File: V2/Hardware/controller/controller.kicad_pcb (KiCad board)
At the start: 2 copper layers, 45 parts, among them J0 Molex_PSU_F, J2 Flat_7seg_F, J3 Rpi_DATA_F_3.3V, Q0 BD139-16, Q1 BD139-16, Q2 BD139-16, Q3 BD139-16, Q4 BD139-16, Q5 BD139-16, Q6 BD139-16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

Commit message: Finish PCBs
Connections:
- net /DATA0 renamed /BIT_D
- J3 pad 2: /DATA1 -> Net-(J3-Pad2)
- J3 pad 3: /DATA2 -> /BIT_C
- J3 pad 4: /DATA3 -> /BIT_C
- J3 pad 5: Net-(J3-Pad5) -> /BIT_B
- J3 pad 6: Net-(J3-Pad6) -> /BIT_A
- R10 pad 2: /DATA1 -> /BIT_C
- R11 pad 2: /DATA2 -> /BIT_B
- R12 pad 2: /DATA3 -> /BIT_A
- U1 pad 7: /DATA1 -> /BIT_C
- U1 pad 8: /DATA2 -> /BIT_B
- U1 pad 9: /DATA3 -> /BIT_A
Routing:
- net /DATA2: track 87.7 -> 0.00 mm, vias 2 -> 0
- net /BIT_B: track 0.00 -> 80.8 mm, vias 0 -> 2
- net /BIT_A: track 0.00 -> 57.9 mm
- net /DATA3: track 52.5 -> 0.00 mm
- net /BIT_C: track 0.00 -> 51.4 mm
- net /DATA1: track 42.4 -> 0.00 mm

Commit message: Reinforce output
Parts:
- J2: footprint Connector_PinHeader_2.54mm:PinHeader_2x04_P2.54mm_Horizontal -> Connector_PinHeader_2.54mm:PinHeader_2x05_P2.54mm_Horizontal
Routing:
- net /+12V: track 183.1 -> 187.3 mm

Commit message: Export -pcbs
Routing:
- net Earth: track 212.7 -> 244.7 mm
- net /+12V: track 187.3 -> 216.8 mm
- net Net-(R0-Pad1): track 169.0 -> 184.9 mm
- net Net-(D5-Pad2): track 14.4 -> 26.7 mm
- net Net-(R18-Pad2): track 44.8 -> 56.3 mm
- net Net-(D6-Pad2): track 9.89 -> 19.1 mm
- net Net-(R19-Pad2): track 55.8 -> 61.4 mm
- net Net-(D4-Pad2): track 8.24 -> 13.2 mm
- net Net-(D2-Pad2): track 9.67 -> 14.3 mm
- net Net-(D3-Pad2): track 9.67 -> 14.0 mm
- net Net-(R16-Pad2): track 23.9 -> 28.2 mm
- net Net-(D1-Pad2): track 8.41 -> 12.4 mm
- net Net-(R1-Pad1): track 16.2 -> 19.5 mm
- net /5V+: track 187.5 -> 190.7 mm
- net Net-(R8-Pad1): track 8.00 -> 11.0 mm
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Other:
- board text added: "BIT 0 1 2 3"
- board text added: "SEGMENT"

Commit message: Update resistor values
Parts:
- R14, R15, R16, R17, R18, R19, R20: value 33k -> 22k

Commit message: Make more precise plots
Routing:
- net (no net): track 0.00 -> 4.00 mm
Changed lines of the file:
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@@
   (general
     (thickness 1.6)
-    (drawings 20)
-    (tracks 424)
+    (drawings 22)
+    (tracks 426)
     (zones 0)
     (modules 45)
@@
     (visible_elements FFFFFF7F)
     (pcbplotparams
-      (layerselection 0x010fc_ffffffff)
+      (layerselection 0x00800_fffffffe)
       (usegerberextensions false)
       (usegerberattributes true)
       (usegerberadvancedattributes true)
       (creategerberjobfile true)
-      (excludeedgelayer true)
+      (excludeedgelayer false)
       (linewidth 0.100000)
       (plotframeref false)
@@
       (psnegative false)
       (psa4output false)
-      (plotreference true)
-      (plotvalue true)
+      (plotreference false)
+      (plotvalue false)
       (plotinvisibletext false)
-      (padsonsilk false)
+      (padsonsilk true)
       (subtractmaskfromsilk false)
-      (outputformat 1)
+      (outputformat 5)
       (mirror false)
       (drillshape 1)
@@
     )
   )
+  (gr_line (start 202 105) (end 202 103) (layer Eco2.User) (width 0.25))
+  (gr_line (start 201 104) (end 203 104) (layer Eco2.User) (width 0.25))
+  (gr_circle (center 206 111) (end 207 112) (layer Eco2.User) (width 0.15))
+  (gr_circle (center 206 111) (end 207 112) (layer Dwgs.User) (width 0.15))
   (gr_text "BIT 0 1 2 3" (at 117 102) (layer Eco2.User)
     (effects (font (size 1 1) (thickness 0.15)))
@@
   (gr_circle (center 89 40) (end 90 39) (layer Eco2.User) (width 0.15))
   (gr_circle (center 89 111) (end 90 110) (layer Eco2.User) (width 0.15))
-  (gr_circle (center 206 111) (end 207 112) (layer Eco2.User) (width 0.15))
   (gr_circle (center 206 40) (end 207 41) (layer Eco2.User) (width 0.15))
   (gr_text 8cm (at 208 74) (layer Eco2.User)
@@
     (effects (font (size 1 1) (thickness 0.15)))
   )
-  (gr_circle (center 206 111) (end 207 112) (layer Dwgs.User) (width 0.15))
   (gr_circle (center 89 40) (end 90 41) (layer Dwgs.User) (width 0.15))
   (gr_circle (center 206 40) (end 207 41) (layer Dwgs.User) (width 0.15))
@@
   (via (at 89 40) (size 0.8) (drill 0.4) (layers F.Cu B.Cu) (net 0))
   (via (at 89 111) (size 0.8) (drill 0.4) (layers F.Cu B.Cu) (net 0))
+  (via (at 206 40) (size 0.8) (drill 0.4) (layers F.Cu B.Cu) (net 0))
   (via (at 206 111) (size 0.8) (drill 0.4) (layers F.Cu B.Cu) (net 0))
-  (via (at 206 40) (size 0.8) (drill 0.4) (layers F.Cu B.Cu) (net 0))
+  (segment (start 202 103) (end 202 105) (width 0.25) (layer B.Cu) (net 0))
+  (segment (start 203 104) (end 201 104) (width 0.25) (layer B.Cu) (net 0))
   (segment (start 113 51.46) (end 115.46 49) (width 1.5) (layer B.Cu) (net 1))
   (segment (start 127 97.54) (end 120 97.54) (width 2) (layer B.Cu) (net 1))

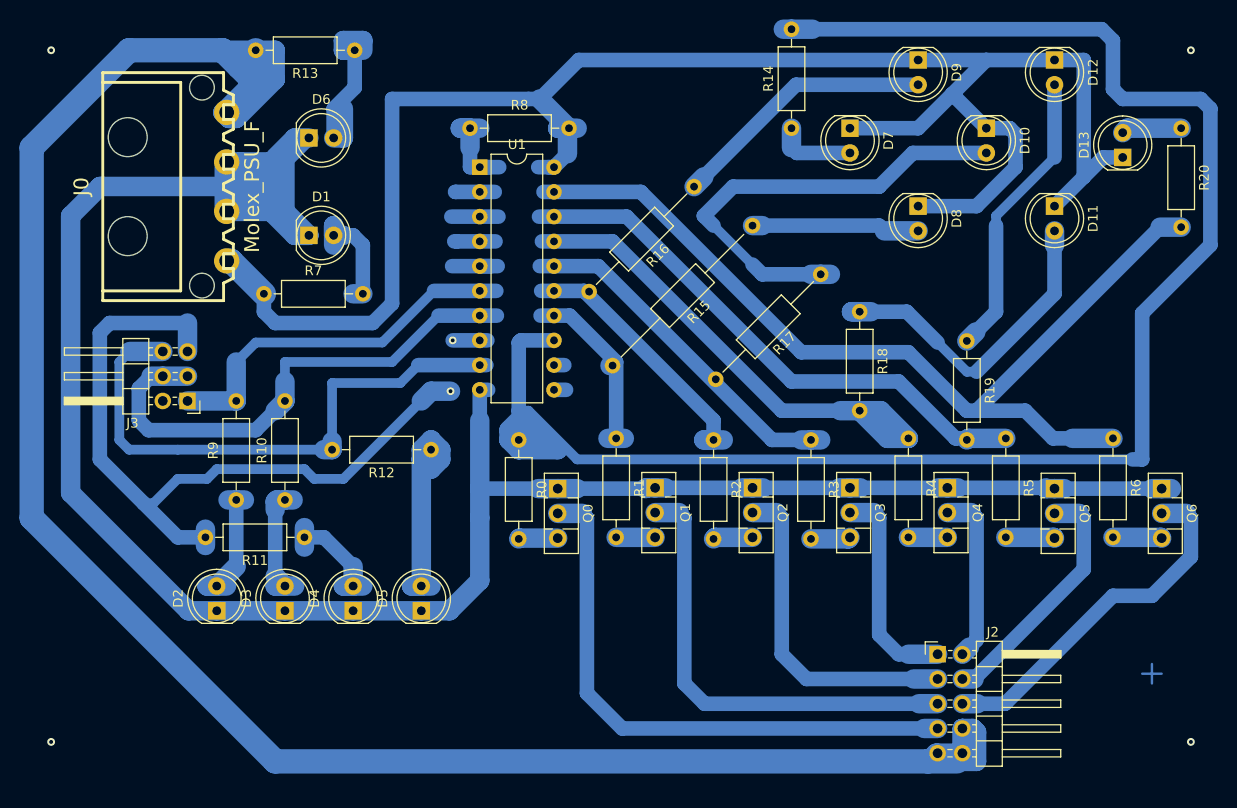
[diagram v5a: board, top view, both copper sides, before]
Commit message: Add bypass caps and filtering
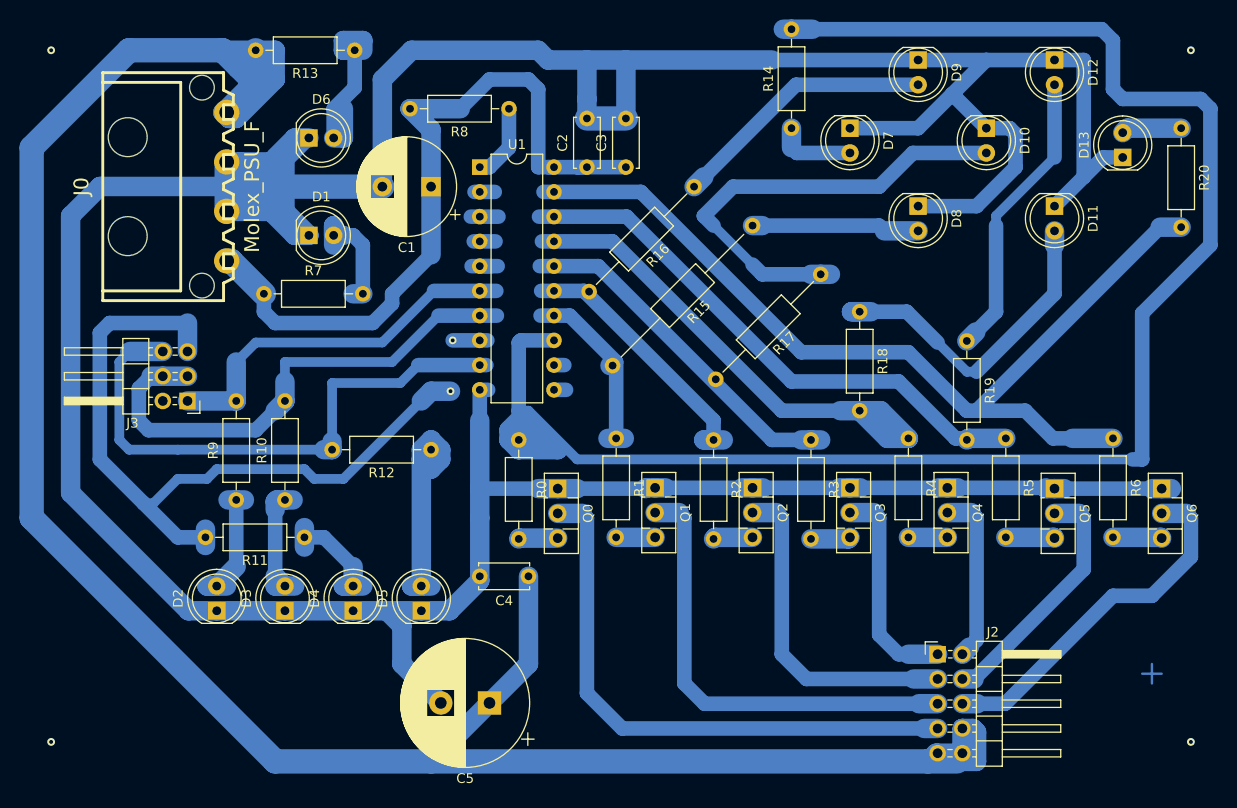
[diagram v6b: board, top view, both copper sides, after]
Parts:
- added C1: 47uF, Capacitor_THT:CP_Radial_D10.0mm_P5.00mm, F.Cu at (128.0, 54.0)
- added C2: 10nF, Capacitor_THT:C_Disc_D5.0mm_W2.5mm_P5.00mm, F.Cu at (144.0, 52.0)
- added C3: 100nF, Capacitor_THT:C_Disc_D5.0mm_W2.5mm_P5.00mm, F.Cu at (148.0, 52.0)
- added C4: 220nF, Capacitor_THT:C_Disc_D5.0mm_W2.5mm_P5.00mm, F.Cu at (138.0, 94.0)
- added C5: 1000uF 35V LOW ESR, Capacitor_THT:CP_Radial_D13.0mm_P5.00mm, F.Cu at (134.0, 107.0)
- moved R8 4.47 mm to (136.0, 46.0), turned to 180 degrees
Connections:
- D10 pad 1: /5V+ -> Earth
- D11 pad 1: /5V+ -> Earth
- D12 pad 1: /5V+ -> Earth
- D13 pad 1: /5V+ -> Earth
- D7 pad 1: /5V+ -> Earth
- D8 pad 1: /5V+ -> Earth
- D9 pad 1: /5V+ -> Earth
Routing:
- net Earth: track 244.7 -> 443.3 mm
- net /5V+: track 190.7 -> 77.5 mm
- net /+12V: track 216.8 -> 239.9 mm
- net Net-(R8-Pad1): track 11.0 -> 7.83 mm
- net Net-(U1-Pad5): track 5.84 -> 3.84 mm
- net Net-(U1-Pad4): track 4.24 -> 2.24 mm
- net Net-(U1-Pad3): track 4.84 -> 2.84 mm
- net Net-(U1-Pad2): track 4.08 -> 2.08 mm

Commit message: Add kicad part lists
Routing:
- net Earth: track 443.3 -> 514.3 mm
